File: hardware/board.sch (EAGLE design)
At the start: 12 parts, among them Q1 FDN360P

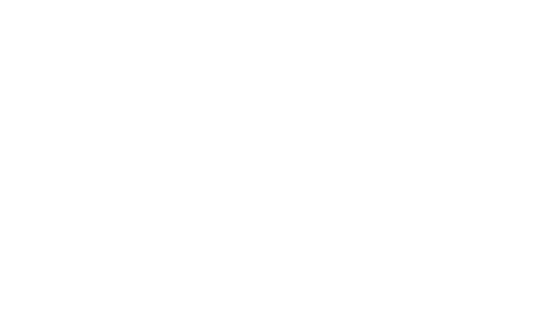
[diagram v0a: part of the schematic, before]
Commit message: Added board revision for makecam
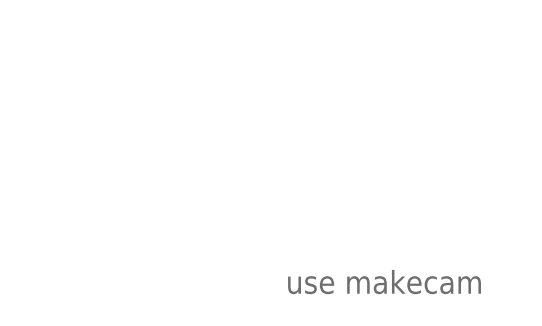
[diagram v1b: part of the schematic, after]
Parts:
- added REV1: (no value), build_light:REVISION
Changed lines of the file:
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@@
 <layer number="48" name="Document" color="7" fill="1" visible="no" active="no"/>
 <layer number="49" name="Reference" color="7" fill="1" visible="no" active="no"/>
+<layer number="50" name="dxf" color="7" fill="1" visible="no" active="no"/>
 <layer number="51" name="tDocu" color="7" fill="1" visible="no" active="no"/>
 <layer number="52" name="bDocu" color="7" fill="1" visible="no" active="no"/>
+<layer number="53" name="tGND_GNDA" color="7" fill="1" visible="no" active="no"/>
+<layer number="54" name="bGND_GNDA" color="7" fill="1" visible="no" active="no"/>
+<layer number="56" name="wert" color="7" fill="1" visible="no" active="no"/>
 <layer number="90" name="Modules" color="5" fill="1" visible="yes" active="yes"/>
 <layer number="91" name="Nets" color="2" fill="1" visible="yes" active="yes"/>
@@
 <layer number="98" name="Guide" color="6" fill="1" visible="yes" active="yes"/>
 <layer number="99" name="SpiceOrder" color="5" fill="1" visible="yes" active="yes"/>
+<layer number="100" name="Mechanical" color="7" fill="1" visible="yes" active="yes"/>
+<layer number="101" name="Gehäuse" color="7" fill="1" visible="yes" active="yes"/>
+<layer number="102" name="Mittellin" color="7" fill="1" visible="yes" active="yes"/>
+<layer number="103" name="ATT_MISO" color="7" fill="1" visible="yes" active="yes"/>
+<layer number="104" name="Name" color="7" fill="1" visible="yes" active="yes"/>
+<layer number="105" name="Beschreib" color="7" fill="1" visible="yes" active="yes"/>
+<layer number="106" name="BGA-Top" color="7" fill="1" visible="yes" active="yes"/>
+<layer number="107" name="BD-Top" color="7" fill="1" visible="yes" active="yes"/>
+<layer number="108" name="centerline" color="7" fill="1" visible="yes" active="yes"/>
+<layer number="116" name="Patch_BOT" color="7" fill="1" visible="yes" active="yes"/>
+<layer number="121" name="_tsilk" color="7" fill="1" visible="yes" active="yes"/>
+<layer number="122" name="_bsilk" color="7" fill="1" visible="yes" active="yes"/>
+<layer number="131" name="prix" color="7" fill="1" visible="yes" active="yes"/>
+<layer number="132" name="test" color="7" fill="1" visible="yes" active="yes"/>
+<layer number="151" name="HeatSink" color="7" fill="1" visible="yes" active="yes"/>
+<layer number="200" name="200bmp" color="7" fill="1" visible="yes" active="yes"/>
+<layer number="201" name="201bmp" color="7" fill="1" visible="yes" active="yes"/>
+<layer number="202" name="202bmp" color="7" fill="1" visible="yes" active="yes"/>
+<layer number="203" name="203bmp" color="7" fill="1" visible="yes" active="yes"/>
+<layer number="204" name="204bmp" color="7" fill="1" visible="yes" active="yes"/>
+<layer number="205" name="205bmp" color="7" fill="1" visible="yes" active="yes"/>
+<layer number="206" name="206bmp" color="7" fill="1" visible="yes" active="yes"/>
+<layer number="207" name="207bmp" color="7" fill="1" visible="yes" active="yes"/>
+<layer number="208" name="208bmp" color="7" fill="1" visible="yes" active="yes"/>
+<layer number="250" name="Descript" color="7" fill="1" visible="yes" active="yes"/>
+<layer number="251" name="SMDround" color="7" fill="1" visible="yes" active="yes"/>
+<layer number="254" name="OrgLBR" color="7" fill="1" visible="yes" active="yes"/>
 </layers>
 <schematic xreflabel="%F%N/%S.%C%R" xrefpart="/%S.%C%R">
 <attributes>
+<attribute name="REVISION" value="use makecam"/>
 </attributes>
 <variantdefs>
@@
 <part name="SUPPLY2" library="supply2" deviceset="+5V" device=""/>
 <part name="D2" library="diode" deviceset="DIODE-" device="SOD323-W"/>
+<part name="REV1" library="build_light" deviceset="REVISION" device=""/>
 </parts>
 <sheets>
@@
 <instance part="SUPPLY2" gate="+5V" x="132.08" y="101.6"/>
 <instance part="D2" gate="G$1" x="93.98" y="109.22"/>
+<instance part="REV1" gate="G$1" x="215.9" y="20.32"/>
 </instances>
 <busses>
